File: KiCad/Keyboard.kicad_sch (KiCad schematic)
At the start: 0 parts

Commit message: Rows, columns, 3.3v, gnd, and en pins
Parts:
- added U1: ESP32-C6-MINI-1, RF_Module:ESP32-C6-MINI-1, symbol RF_Module:ESP32-C6-MINI-1
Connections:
- new net +3.3V: U1.3 (3V3), U1.8 (EN)
- new net COL_0: U1.24 (IO18)
- new net COL_1: U1.25 (IO19)
- new net COL_2: U1.26 (IO20)
- new net COL_3: U1.27 (IO21)
- new net COL_4: U1.28 (IO22)
- new net GND: U1.1 (GND), U1.11 (GND), U1.14 (GND), U1.2 (GND), U1.36 (GND), U1.37 (GND), U1.38 (GND), U1.39 (GND), U1.40 (GND), U1.41 (GND), U1.42 (GND), U1.43 (GND), U1.44 (GND), U1.45 (GND), U1.46 (GND), U1.47 (GND), U1.48 (GND), U1.49 (GND), U1.50 (GND), U1.51 (GND), U1.52 (GND), U1.53 (GND)
- new net ROW_0: U1.12 (IO0)
- new net ROW_1: U1.13 (IO1)
- new net ROW_2: U1.5 (IO2)
- new net ROW_3: U1.6 (IO3)
- new net ROW_4: U1.9 (IO4)
- new net ROW_5: U1.10 (IO5)
- new net ROW_6: U1.15 (IO6)

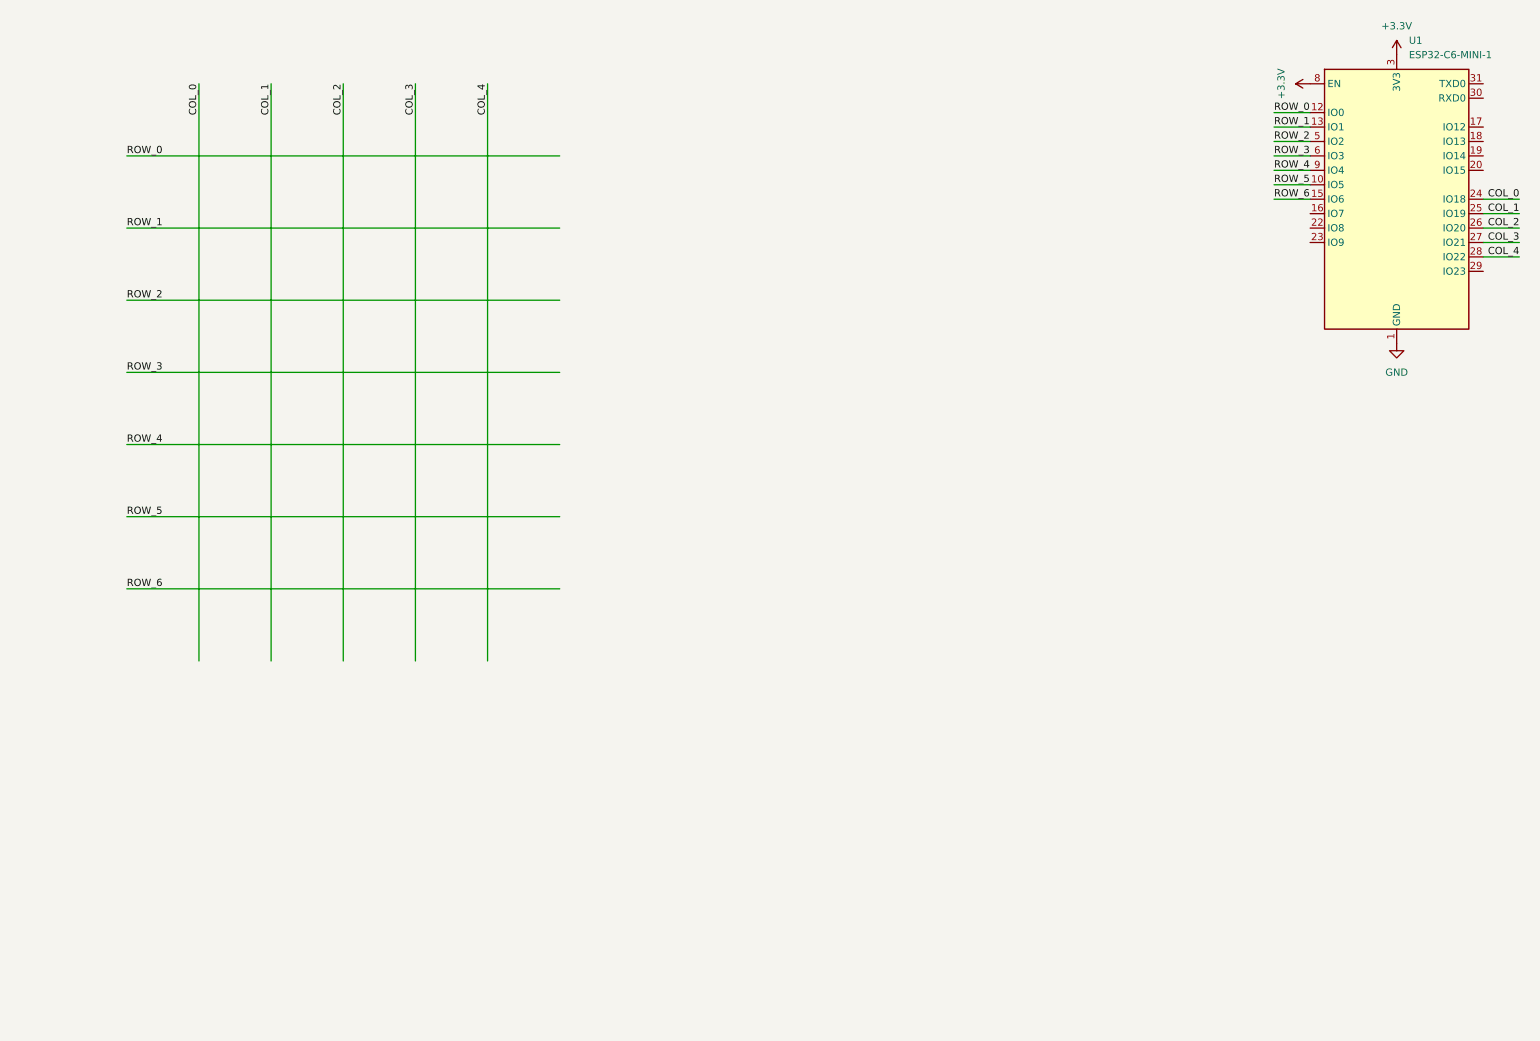
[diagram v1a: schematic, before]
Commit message: Switches and diodes
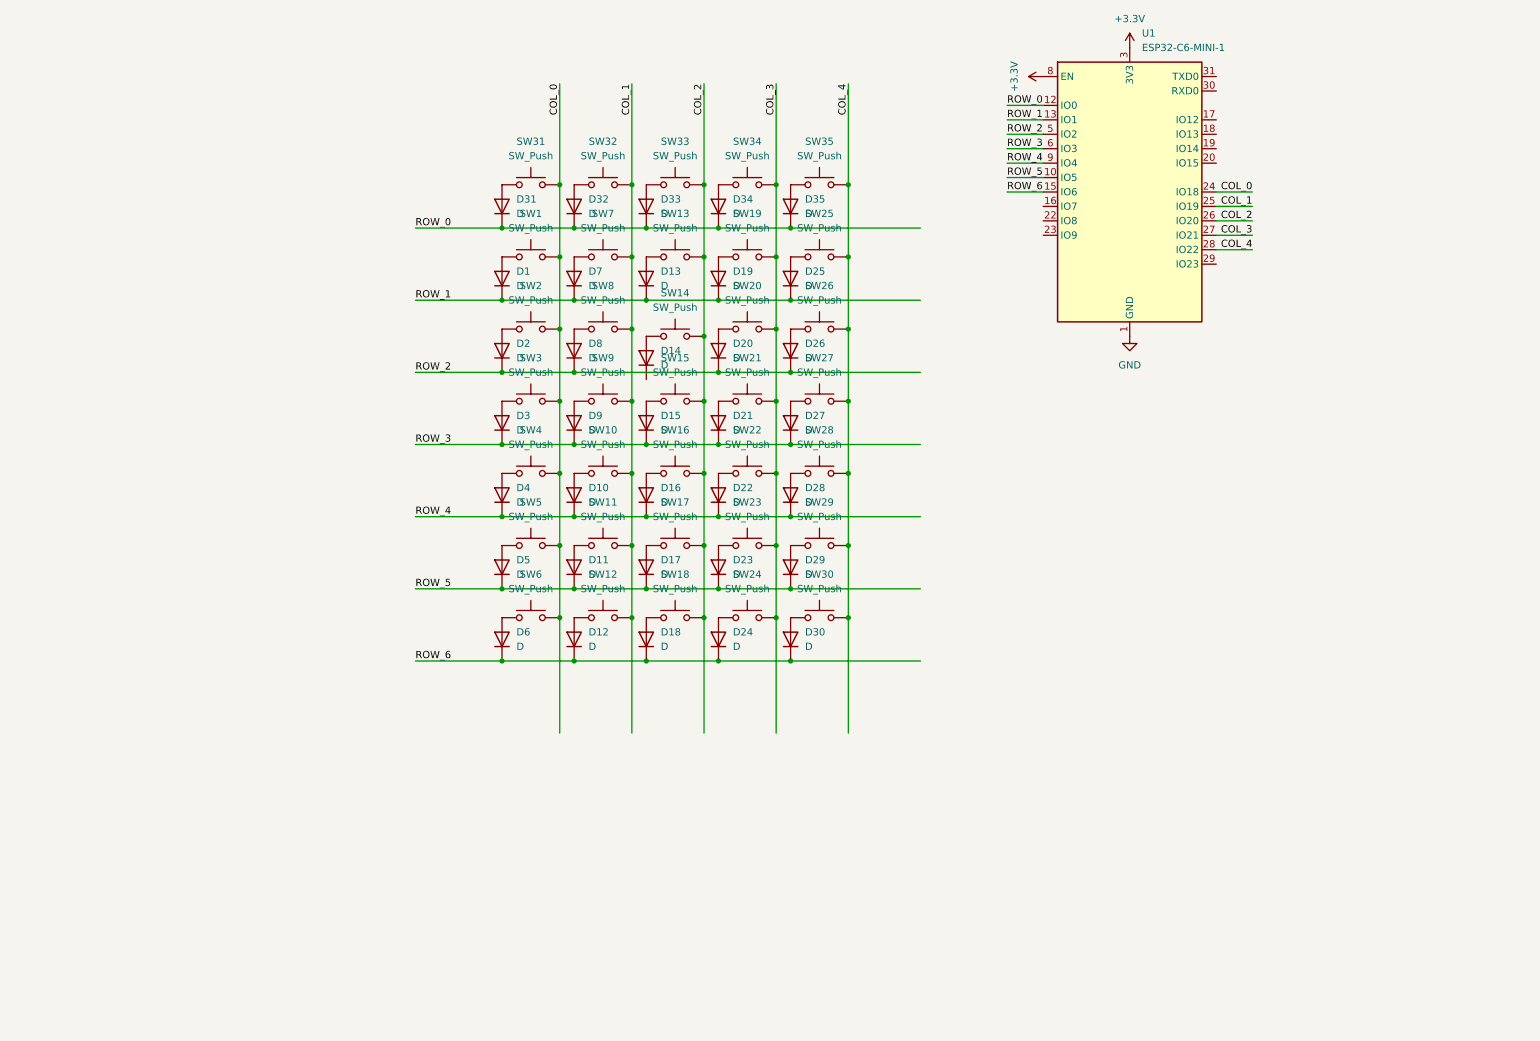
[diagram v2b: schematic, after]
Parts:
- added D1, D10, D11, D12, D13, D14, D15, D16, D17, D18, D19, D2, D20, D21, D22, D23, D24, D25, D26, D27, D28, D29, D3, D30, D31, D32, D33, D34, D35, D4, D5, D6, D7, D8, D9: D, symbol Device:D
- added SW1, SW10, SW11, SW12, SW13, SW14, SW15, SW16, SW17, SW18, SW19, SW2, SW20, SW21, SW22, SW23, SW24, SW25, SW26, SW27, SW28, SW29, SW3, SW30, SW31, SW32, SW33, SW34, SW35, SW4, SW5, SW6, SW7, SW8, SW9: SW_Push, symbol Switch:SW_Push
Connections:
- net COL_0: now also SW1.2, SW2.2, SW3.2, SW31.2, SW4.2, SW5.2, SW6.2
- net COL_1: now also SW10.2, SW11.2, SW12.2, SW32.2, SW7.2, SW8.2, SW9.2
- net COL_2: now also SW13.2, SW14.2, SW15.2, SW16.2, SW17.2, SW18.2, SW33.2
- net COL_3: now also SW19.2, SW20.2, SW21.2, SW22.2, SW23.2, SW24.2, SW34.2
- net COL_4: now also SW25.2, SW26.2, SW27.2, SW28.2, SW29.2, SW30.2, SW35.2
- net ROW_0: now also D31.1 (K), D32.1 (K), D33.1 (K), D34.1 (K), D35.1 (K)
- net ROW_1: now also D1.1 (K), D13.1 (K), D19.1 (K), D25.1 (K), D7.1 (K)
- net ROW_2: now also D2.1 (K), D20.1 (K), D26.1 (K), D8.1 (K)
- net ROW_3: now also D15.1 (K), D21.1 (K), D27.1 (K), D3.1 (K), D9.1 (K)
- net ROW_4: now also D10.1 (K), D16.1 (K), D22.1 (K), D28.1 (K), D4.1 (K)
- net ROW_5: now also D11.1 (K), D17.1 (K), D23.1 (K), D29.1 (K), D5.1 (K)
- net ROW_6: now also D12.1 (K), D18.1 (K), D24.1 (K), D30.1 (K), D6.1 (K)
- new net: D35.2 (A), SW35.1
- new net: D4.2 (A), SW4.1
- new net: D6.2 (A), SW6.1
- new net: D9.2 (A), SW9.1
- new net: D12.2 (A), SW12.1
- new net: D5.2 (A), SW5.1
- new net: D14.2 (A), SW14.1
- new net: D32.2 (A), SW32.1
- new net: D24.2 (A), SW24.1
- new net: D22.2 (A), SW22.1
- new net: D23.2 (A), SW23.1
- new net: D18.2 (A), SW18.1
- new net: D1.2 (A), SW1.1
- new net: D25.2 (A), SW25.1
- new net: D16.2 (A), SW16.1
- new net: D34.2 (A), SW34.1
- new net: D13.2 (A), SW13.1
- new net: D29.2 (A), SW29.1
- new net: D3.2 (A), SW3.1
- new net: D17.2 (A), SW17.1
- new net: D31.2 (A), SW31.1
- new net: D20.2 (A), SW20.1
- new net: D21.2 (A), SW21.1
- new net: D10.2 (A), SW10.1
- new net: D11.2 (A), SW11.1
- new net: D15.2 (A), SW15.1
- new net: D8.2 (A), SW8.1
- new net: D26.2 (A), SW26.1
- new net: D28.2 (A), SW28.1
- new net: D7.2 (A), SW7.1
- new net: D30.2 (A), SW30.1
- new net: D33.2 (A), SW33.1
- new net: D2.2 (A), SW2.1
- new net: D27.2 (A), SW27.1
- new net: D19.2 (A), SW19.1
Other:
- moved on the sheet: U1

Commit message: Fix flipped count for rows/cols
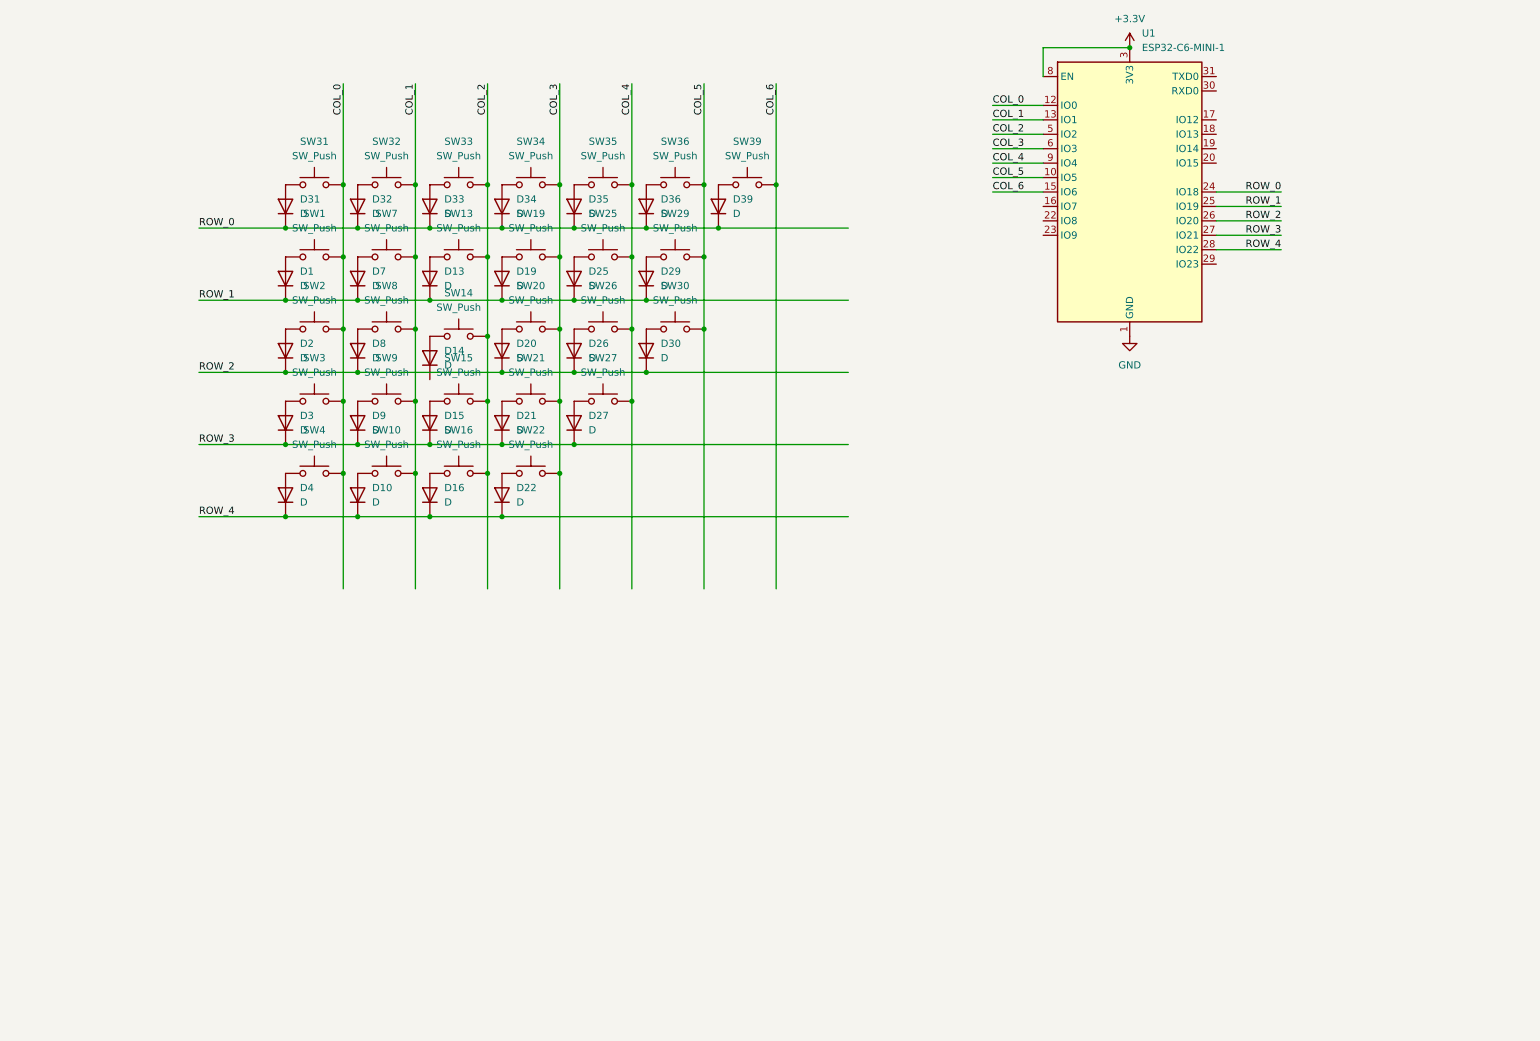
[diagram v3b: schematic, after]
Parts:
- removed D11, D12, D17, D18, D23, D24, D28, D5, D6: D, symbol Device:D
- removed SW11, SW12, SW17, SW18, SW23, SW24, SW28, SW5, SW6: SW_Push, symbol Switch:SW_Push
- added D36, D39: D, symbol Device:D
- added SW36, SW39: SW_Push, symbol Switch:SW_Push
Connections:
- net COL_0: now also U1.12 (IO0); no longer U1.24 (IO18)
- net COL_1: now also U1.13 (IO1); no longer U1.25 (IO19)
- net COL_2: now also U1.5 (IO2); no longer U1.26 (IO20)
- net COL_3: now also U1.6 (IO3); no longer U1.27 (IO21)
- net COL_4: now also U1.9 (IO4); no longer SW29.2, SW30.2, U1.28 (IO22)
- net ROW_0: now also U1.24 (IO18), D36.1 (K), D39.1 (K); no longer U1.12 (IO0)
- net ROW_1: now also D29.1 (K), U1.25 (IO19); no longer U1.13 (IO1)
- net ROW_2: now also D30.1 (K), U1.26 (IO20); no longer U1.5 (IO2)
- net ROW_3: now also U1.27 (IO21); no longer U1.6 (IO3)
- net ROW_4: now also U1.28 (IO22); no longer U1.9 (IO4)
- net ROW_5 renamed COL_5
- net COL_5: now also SW29.2, SW30.2, SW36.2; no longer D29.1 (K)
- net ROW_6 renamed COL_6
- net COL_6: now also SW39.2; no longer D30.1 (K)
- new net: D36.2 (A), SW36.1
- new net: D39.2 (A), SW39.1
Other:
- moved on the sheet: D1, D10, D13, D14, D15, D16, D19, D2, D20, D21, D22, D25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

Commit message: Power smoothing + reset circuit
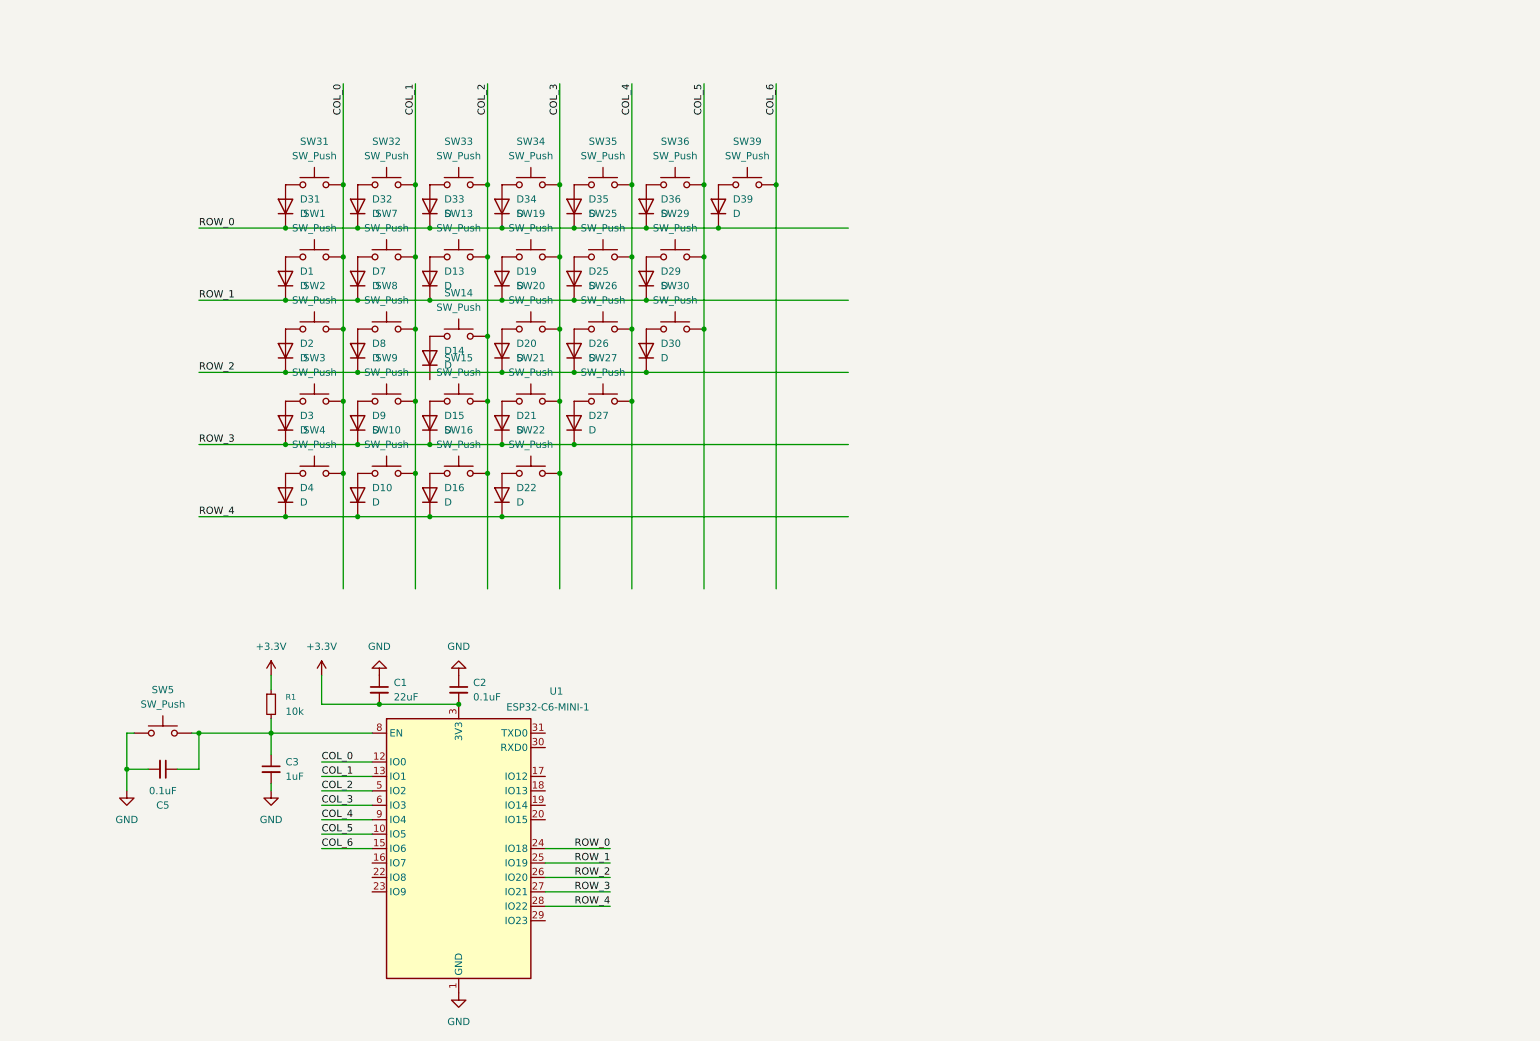
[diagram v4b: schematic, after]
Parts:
- added C1: 22uF, symbol Device:C_Small
- added C2, C5: 0.1uF, symbol Device:C_Small
- added C3: 1uF, symbol Device:C_Small
- added R1: 10k, symbol Device:R_Small
- added SW5: SW_Push, symbol Switch:SW_Push
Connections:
- net +3.3V: now also C1.2, C2.2, R1.1; no longer U1.8 (EN)
- net GND: now also C1.1, C2.1, C3.2, C5.2, SW5.1
- new net: C3.1, C5.1, R1.2, SW5.2, U1.8 (EN)
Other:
- moved on the sheet: U1

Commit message: Wire up USB receptacle
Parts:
- added C4: ???, symbol Device:C_Small
- added J1: USB_C_Receptacle, symbol Connector:USB_C_Receptacle
- added R2, R3: 5.1k, symbol Device:R_Small
- added U2: USBLC6-2SC6, Package_TO_SOT_SMD:SOT-23-6, symbol Power_Protection:USBLC6-2SC6
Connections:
- net GND: now also C4.2, J1.A1 (GND), J1.A12 (GND), J1.B1 (GND), J1.B12 (GND), J1.SH (SHIELD), R2.1, R3.1, U2.2 (GND)
- net USB_D-: now reaches U1.17 (IO12)
- net USB_D-: now also U2.6 (I/O1)
- net USB_D+: now reaches U1.18 (IO13)
- net USB_D+: now also U2.4 (I/O2)
- new net: J1.A5 (CC1), R2.2
- new net: J1.B5 (CC2), R3.2
- new net +5V: C4.1, J1.A4 (VBUS), J1.A9 (VBUS), J1.B4 (VBUS), J1.B9 (VBUS), U2.5 (VBUS)
- new net D+: J1.A6 (D+), J1.B6 (D+), U2.3 (I/O2)
- new net D-: J1.A7 (D-), J1.B7 (D-), U2.1 (I/O1)
- no-connect marks 0 -> 10

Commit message: Wire up OLED
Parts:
- added Brd1: SSD1306, symbol SSD1306-128x64_OLED:SSD1306
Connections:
- net +3.3V: now also Brd1.2 (VCC)
- net GND: now also Brd1.1 (GND)
- net OLED_SCL: now reaches U1.19 (IO14)
- net OLED_SCL: now also Brd1.3 (SCL)
- net OLED_SDA: now reaches U1.20 (IO15)
- net OLED_SDA: now also Brd1.4 (SDA)
- no-connect marks 10 -> 14
